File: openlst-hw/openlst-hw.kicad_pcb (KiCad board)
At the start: 4 copper layers, 80 x 80 mm, 194 parts, among them J1 Conn_02x03_Pin, J10 RJ45_Amphenol_RJMG1BD3B8K1ANR, J11 10155435-00011LF, J12 Conn_01x05_Pin Vertical, J13 Conn_01x04_Pin Vertical, J2 Conn_01x06_Pin, J3 Conn_01x03_Pin, J4 Conn_01x03_Pin, J5 SMA Jack, J6 Conn_01x03_Pin, J7 SMA Jack, J8 PC104 Conn_02x20_Odd_Even, J9 Conn_01x05_Pin, SW1 EVP-AA602W, SW2 EVP-AA602W, U1 CC1110, U10 INA226AIDGSR, U11 W5500, U12 TPS22968QDMGRQ1, U13 STM32L496RGTx, U14 74LVC2G07, U15 MR25H10, U16 TPS22968QDMGRQ1, U2 TA1808A, U3 PE4250MLI, U4 PE4250MLI, U5 0433BM15A0001, U6 RFFM6406, U7 TCAN3414, U8 TCAN3414, U9 MCP23008T-E/SS, X1 27MHz, X2 10MHz, X3 25MHz, X4 32.768KHZ

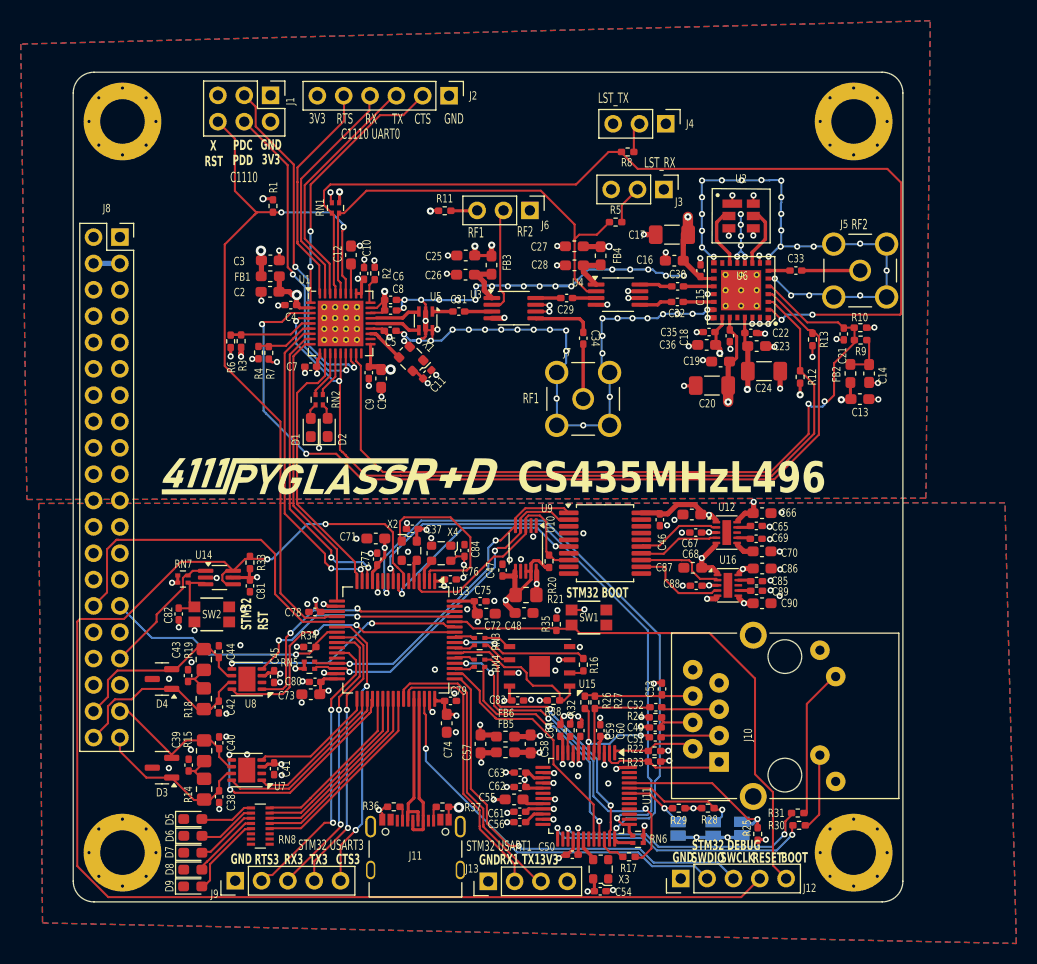
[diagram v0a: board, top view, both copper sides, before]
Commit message: cleanup pullups for reset and schmitt trigger for reset; select available thermal NTCs for avi board and use chip for voltage dividers
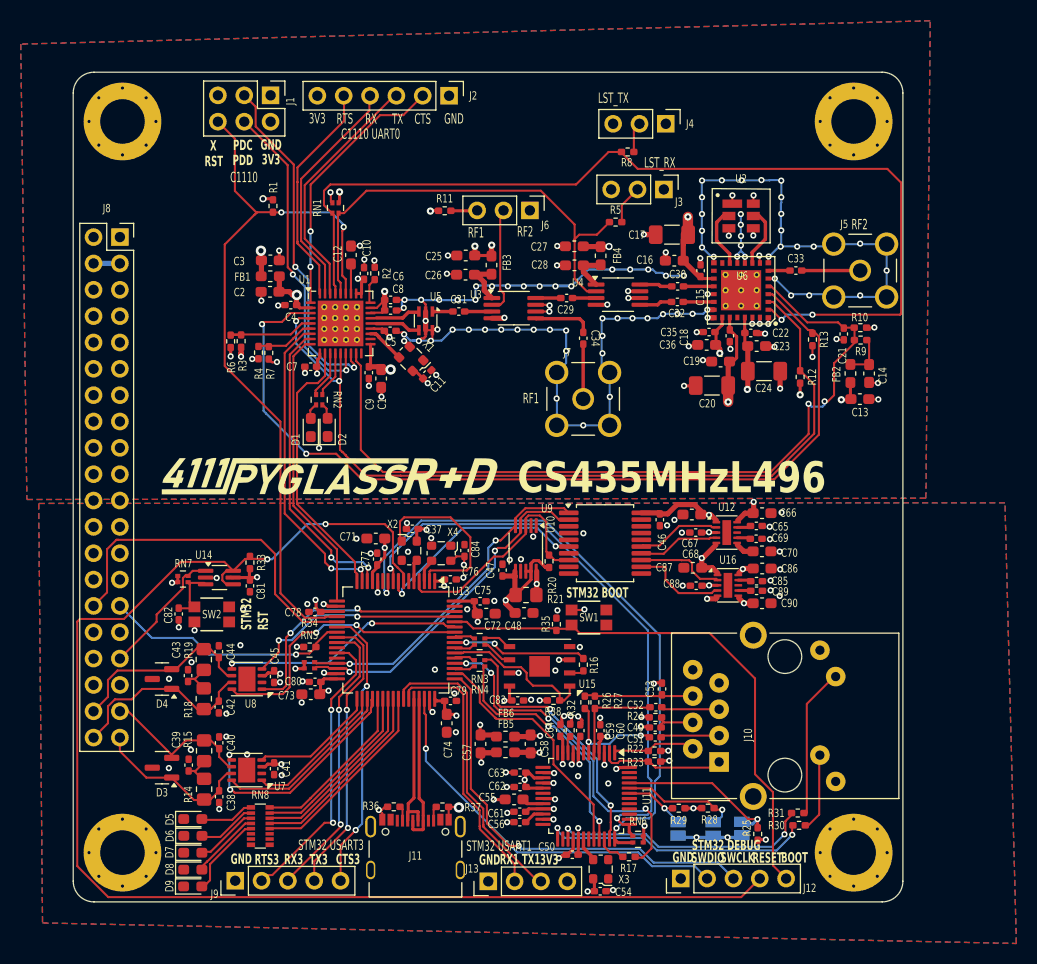
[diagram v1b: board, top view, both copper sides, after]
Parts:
- RN1, RN2, RN3, RN4, RN5, RN6, RN7: footprint Resistor_SMD:R_Array_Convex_2x0402 -> Common:R_Array_Convex_2x0402_widepads
- RN8: footprint Resistor_SMD:R_Array_Convex_8x0602 -> Common:R_Array_Convex_8x0602_widepads

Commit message: checked BOM for sci wo switches
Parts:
- moved C46 0.12 mm to (116.6, 103.3)
- moved C47 0.12 mm to (101.4, 108.1)
- moved C48 0.12 mm to (103.5, 112.2)
- moved C65 0.12 mm to (125.9, 103.9)
- moved C66 0.12 mm to (126.5, 102.6)
- moved C67 0.12 mm to (119.7, 102.8)
- moved C68 0.12 mm to (120.1, 104.5)
- moved C69 0.12 mm to (125.9, 105.1)
- moved C70 0.12 mm to (126.5, 106.3)
- moved C85 0.12 mm to (125.9, 109.2)
- moved C87 0.12 mm to (119.8, 107.9)
- moved C88 0.12 mm to (120.1, 109.6)
- moved C89 0.12 mm to (125.9, 110.1)
- moved C90 0.12 mm to (126.5, 111.3)
- moved R20 0.12 mm to (105.9, 107.3)
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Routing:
- net /GND: vias 188 -> 187

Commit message: power traces and vias of AUX and SCIlite are 0,5mm and 0.5/1.0mm
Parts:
- D5: value LED_SMD_RED -> RED
- D6: value LED_SMD_GREEN -> GREEN
- D7, D8, D9: value LED_SMD_YELLOW -> YELLOW
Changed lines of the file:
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@@
 			)
 		)
-		(property "Description" "SWITCH TACTILE SPST-NO 0.02A 15V"
+		(property "Description" "SPST"
 			(at 0 0 0)
 			(layer "F.Fab")
@@
 			)
 		)
-		(property "Value" "LED_SMD_YELLOW"
+		(property "Value" "YELLOW"
 			(at 0 1.43 0)
 			(unlocked yes)
@@
 			)
 		)
-		(property "Value" "LED_SMD_YELLOW"
+		(property "Value" "YELLOW"
 			(at 0 1.43 0)
 			(unlocked yes)
@@
 			)
 		)
-		(property "Description" "TVS DIODE 24VWM 44VC SOT23-3"
+		(property "Description" "Dual TVS diode"
 			(at 0 0 180)
 			(unlocked yes)
@@
 			)
 		)
-		(property "Value" "LED_SMD_RED"
+		(property "Value" "RED"
 			(at 0 1.43 0)
 			(unlocked yes)
@@
 			)
 		)
-		(property "Value" "LED_SMD_YELLOW"
+		(property "Value" "YELLOW"
 			(at 0 1.43 0)
 			(unlocked yes)
@@
 			)
 		)
-		(property "Description" "TVS DIODE 24VWM 44VC SOT23-3"
+		(property "Description" "Dual TVS diode"
 			(at 0 0 180)
 			(unlocked yes)
@@
 			)
 		)
-		(property "Value" "LED_SMD_GREEN"
+		(property "Value" "GREEN"
 			(at 0 1.43 0)
 			(unlocked yes)

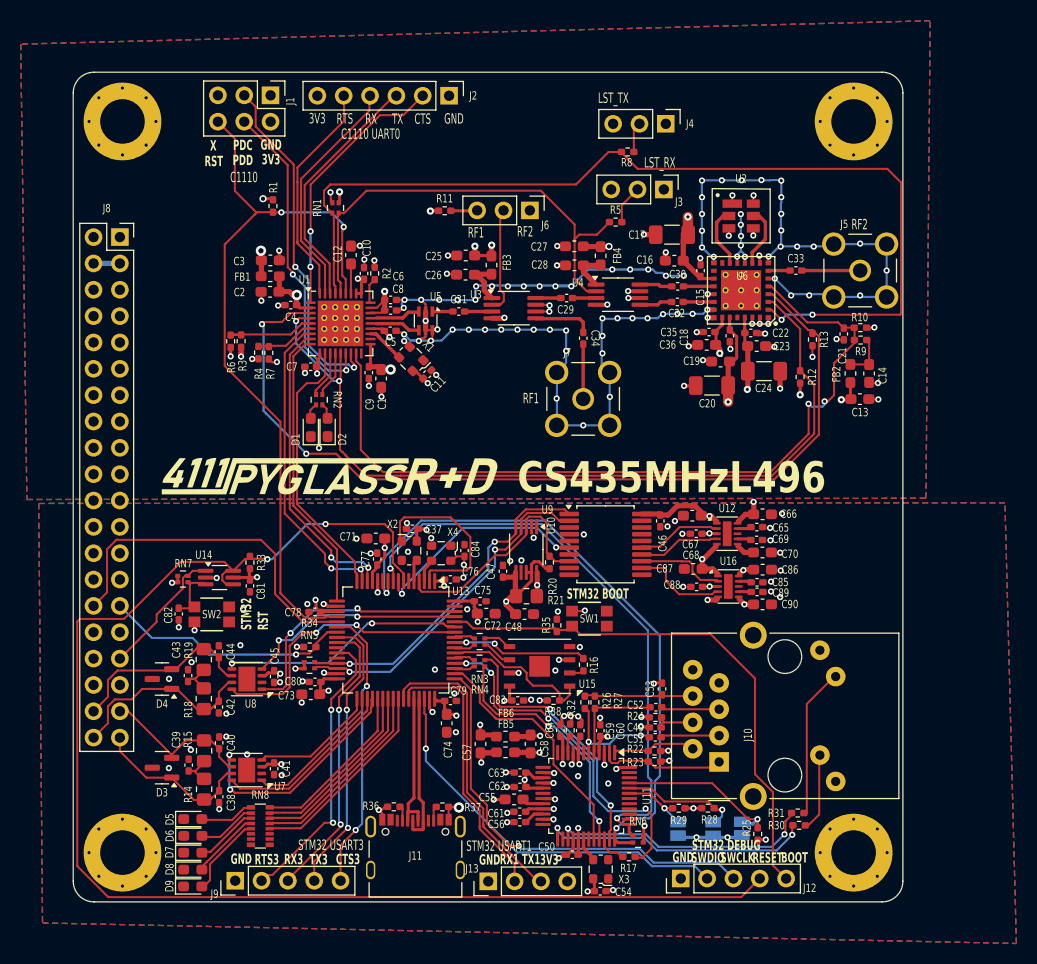
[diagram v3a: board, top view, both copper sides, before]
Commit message: move SPI CS pullups to outer schema to combine multiple with RNs
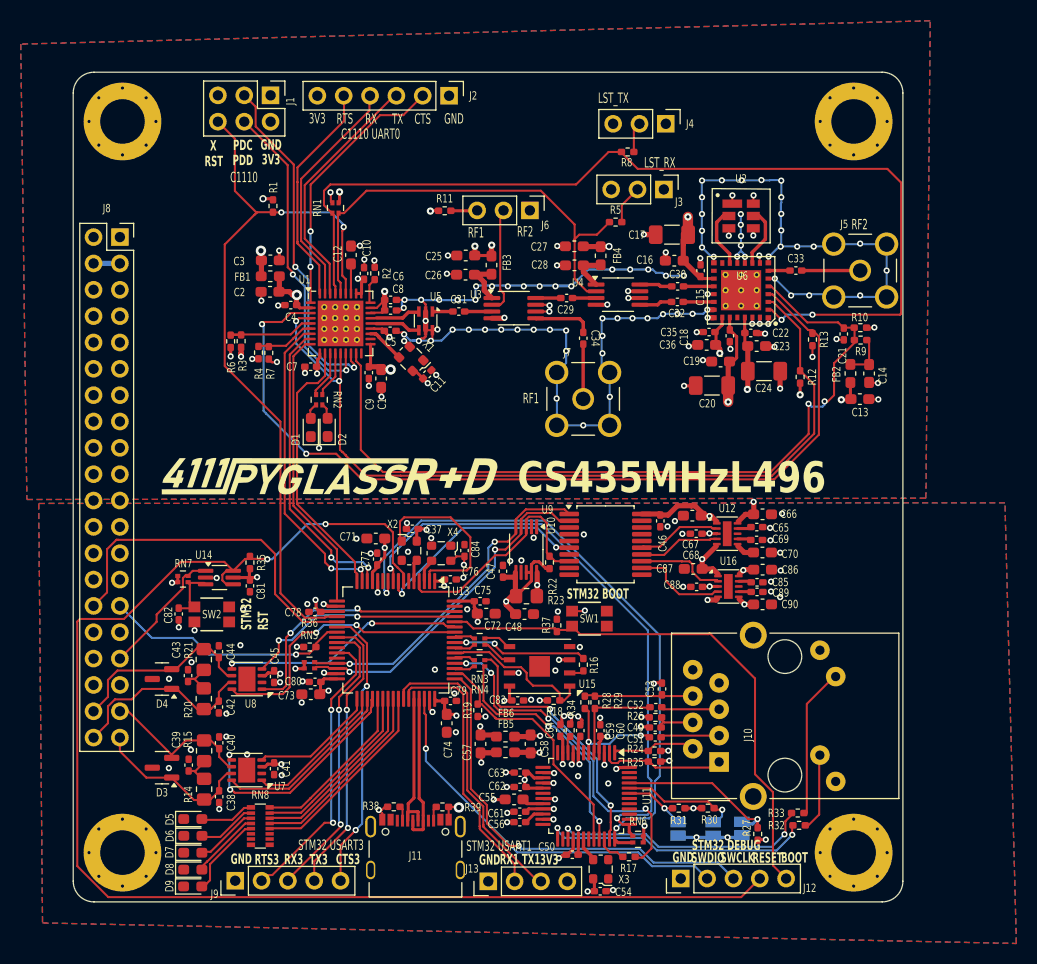
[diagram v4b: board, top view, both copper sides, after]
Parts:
- removed the R38 at (106.3, 120.6)
- added R18: 100K, Resistor_SMD:R_0402_1005Metric_Pad0.72x0.64mm_HandSolder, F.Cu at (106.3, 120.6)
- added R19: 100K, Resistor_SMD:R_0402_1005Metric_Pad0.72x0.64mm_HandSolder, F.Cu at (99.0, 121.5)
- C39, C43: value 4.7nF -> 4nF7
- D1: value LED_SMD_GREEN -> GREEN
- D2: value LED_SMD_YELLOW -> YELLOW
- renumbered R18 to R20, R19 to R21, R20 to R22, R21 to R23, R22 to R24, R23 to R25, R24 to R26, R25 to R27, R26 to R28, R27 to R29, R28 to R30, R29 to R31, R30 to R32, R31 to R33, R32 to R34, R33 to R35, R34 to R36, R35 to R37, R36 to R38, R37 to R39
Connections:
- net /CAN Bridge/MRAM/SPI_CS renamed /CAN Bridge/SPI1_CS_MRAM
- net /CAN Bridge/PMIC/SPI3_CS_FLASH renamed /CAN Bridge/SPI1_CS_LAN
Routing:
- net /3V3_LAN: track 99.2 -> 104.8 mm, vias 7 -> 8
- net /MCU/UART0_RTS: track 22.3 -> 21.5 mm
- net /CAN Bridge/SPI_LAN/AGND: track 18.5 -> 17.7 mm
- net /MCU/UART0_RX: track 23.5 -> 22.9 mm
